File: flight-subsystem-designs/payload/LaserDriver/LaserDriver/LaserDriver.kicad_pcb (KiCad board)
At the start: 4 copper layers, 80.9 x 71 mm, 56 parts, among them J1 Laser 0, J2 Laser 1, J3 Input, J4 BNC, J5 VIN Banana, J6 VIN Pin Header, J7 GND Banana, U1 MAX3967AETG+, U2 DPC6137, U3 MAX3967AETG+, U4 74LVC1G04, U5 SY100ELT22ZG-TR, U6 LDL212PV33R, U7 UCC33420RAQR

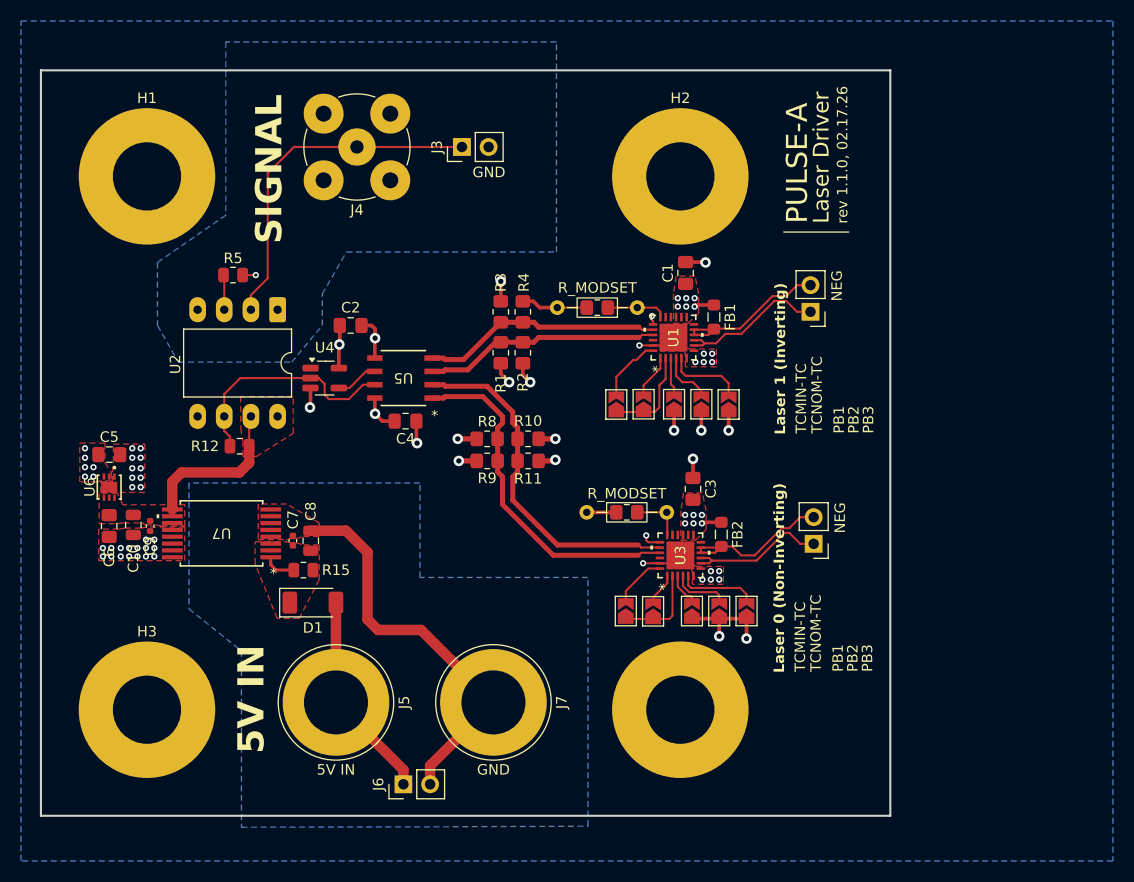
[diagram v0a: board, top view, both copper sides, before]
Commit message: ld: v1.2.0; new LDO, corrected isopower footprint, disspation res
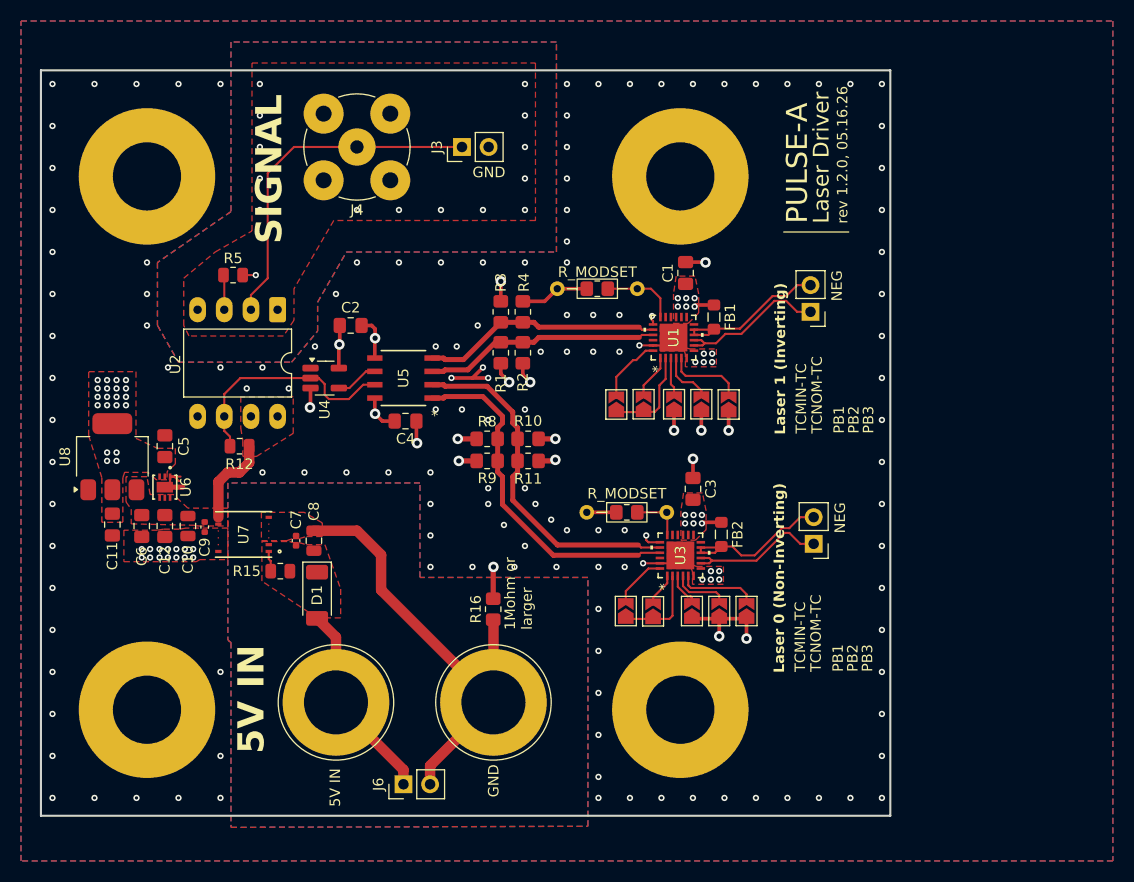
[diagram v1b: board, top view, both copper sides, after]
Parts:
- added C11: 4.7uF, Capacitor_SMD:C_0805_2012Metric_Pad1.18x1.45mm_HandSolder, F.Cu at (123.7, 84.0)
- added C12: 1uF, Capacitor_SMD:C_0805_2012Metric_Pad1.18x1.45mm_HandSolder, F.Cu at (128.7, 84.1)
- added R16: 1M+, Resistor_SMD:R_0805_2012Metric_Pad1.20x1.40mm_HandSolder, F.Cu at (160.0, 92.0)
- added U8: LDL1117S33R, Package_TO_SOT_SMD:SOT-223-3_TabPin2, F.Cu at (123.7, 77.5)
- U7: value UCC33420RAQR -> PUCC33420QRAQRQ1; footprint footprints:SSOP16_DHA_TEX -> footprints:VSON-FCRLF12_RAQ_TEX
- moved C5 5.35 mm to (128.7, 76.5), turned to 90 degrees
- moved U6 5.30 mm to (128.7, 80.4)
- moved C9 5.20 mm to (132.5, 84.2)
- moved C10 5.20 mm to (130.9, 84.1)
- moved C6 3.10 mm to (126.5, 84.1)
- moved R15 2.20 mm to (139.7, 88.4)
- moved U7 2.10 mm to (136.2, 84.9)
- moved R6 1.80 mm to (169.9, 61.5)
- moved R7 1.80 mm to (173.7, 61.5)
- moved D1 0.81 mm to (143.2, 90.7), turned to -90 degrees
- moved C7 0.30 mm to (141.2, 85.5)
- moved C8 0.30 mm to (142.9, 85.5)
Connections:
- U7 pad 10: +5V -> GND
- U7 pad 11: +5V -> GND
- U7 pad 3: /Power Input and Filtering/VIN -> /Power Input and Filtering/RAW_GND
- U7 pad 7: /Power Input and Filtering/RAW_GND -> +5V
- U7 pad 8: /Power Input and Filtering/RAW_GND -> +5V
- U7 pad 9: +5V -> GND
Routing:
- net GND: track 45.9 -> 59.1 mm, vias 51 -> 171
- net +5V: track 15.2 -> 8.63 mm
- net /Power Input and Filtering/RAW_GND: track 38.2 -> 44.0 mm
- net Net-(U1-MODSET): track 5.68 -> 7.19 mm
- net Net-(U7-EN/FLT): track 3.13 -> 1.95 mm
- net Net-(D1-A): track 20.0 -> 19.2 mm
- net /SIGNAL_GND: vias 1 -> 15
- net +3V3: vias 26 -> 40
- added copper zone on F.Cu, net /SIGNAL_GND
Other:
- board text added: "1Mohm or larger"
- board text added: "rev 1.2.0, 05.16.26"
- board text removed: "rev 1.1.0, 02.17.26"
